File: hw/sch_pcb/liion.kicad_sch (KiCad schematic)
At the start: 64 parts, among them Q4 BC817-25, Q5 BC807-25, SW4 SKRTLAE010, U1 BQ34Z100, U13 BQ25628E, U2 SN74HC164D

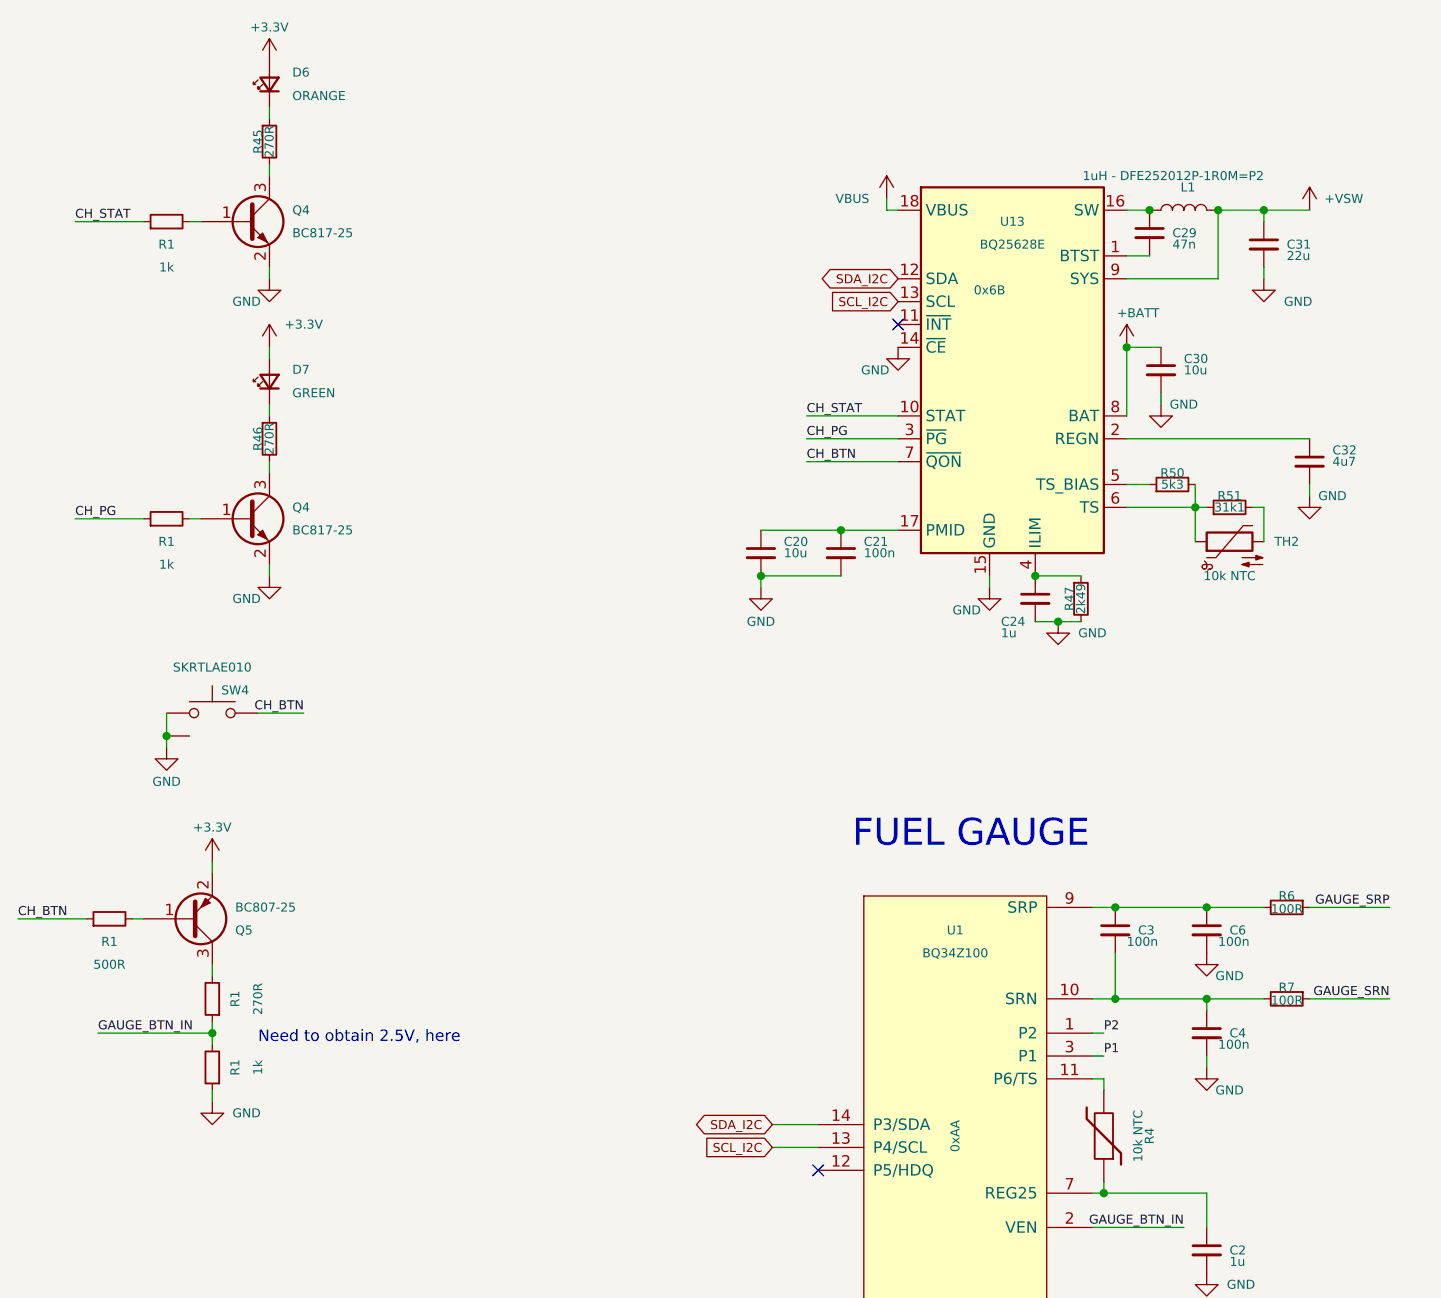
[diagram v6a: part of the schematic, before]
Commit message: minor updates, update kibot
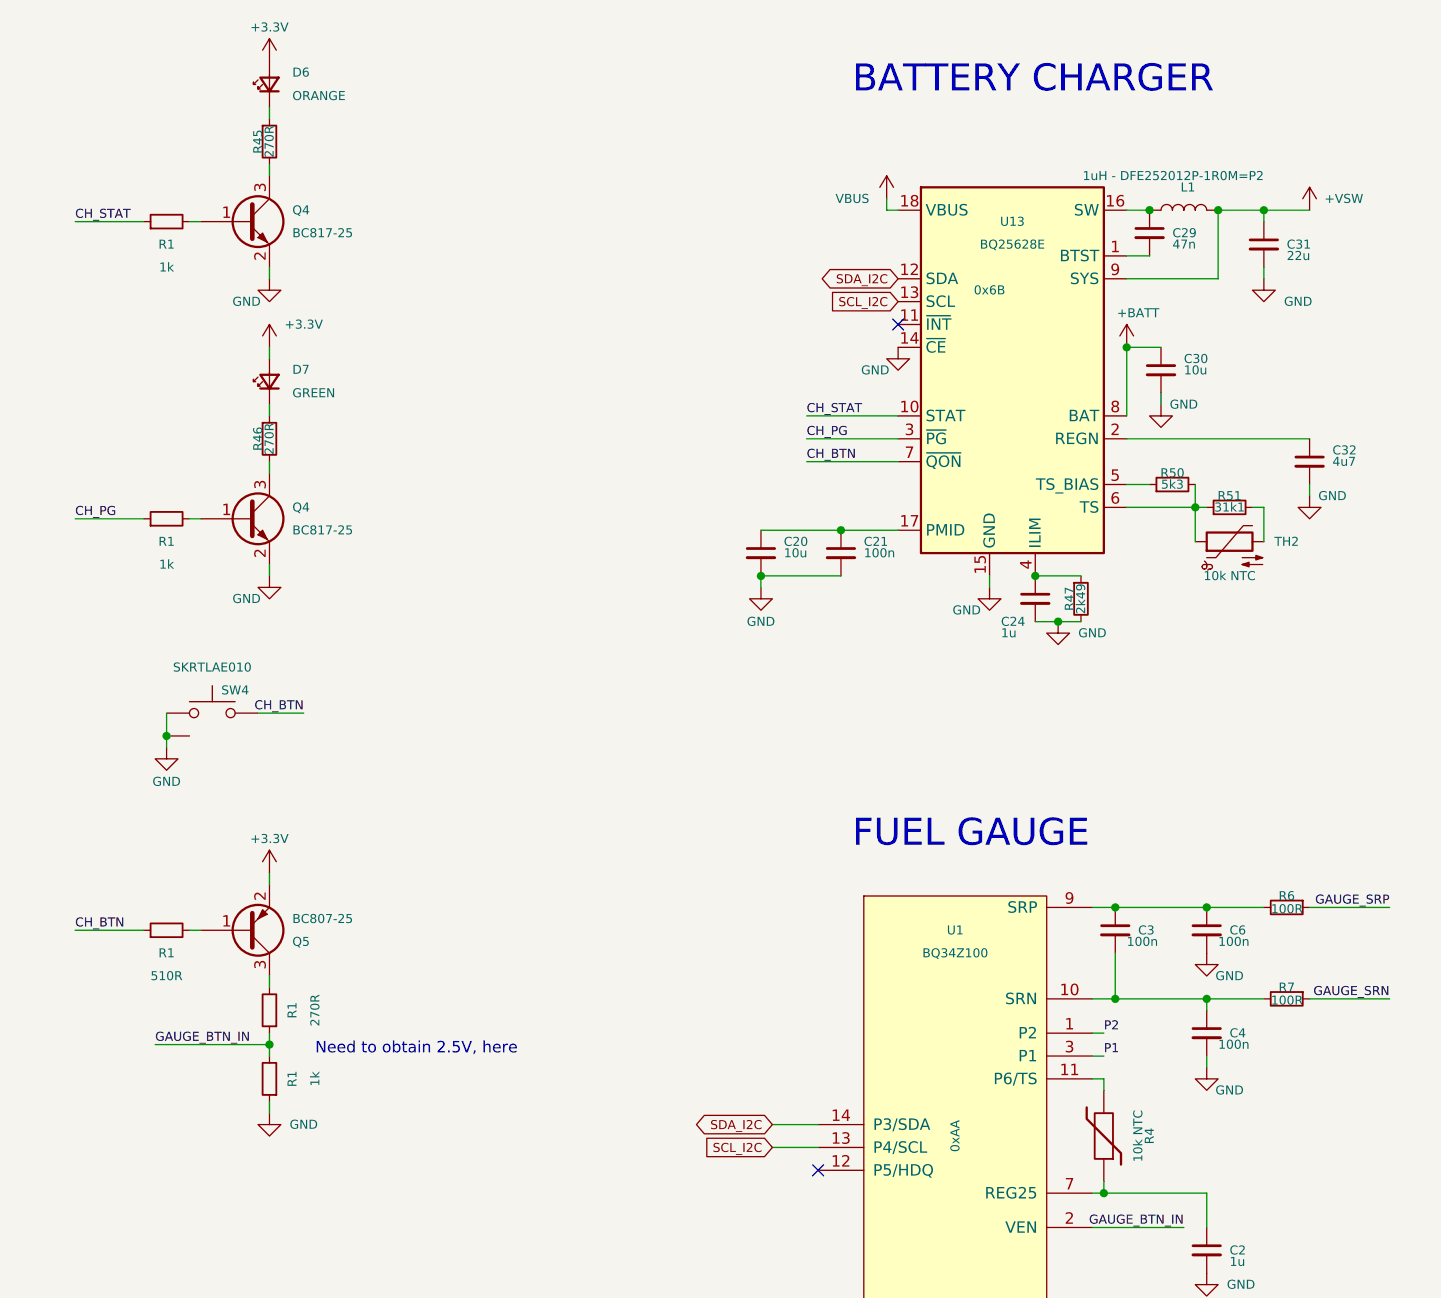
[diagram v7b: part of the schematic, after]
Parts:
- C29: UST_ID (none) -> 65482046462c6d9e72056b98
- D1, D2: UST_ID (none) -> 65481f96462c6d9e72056b54
- D3, D4, D5, D7: UST_ID (none) -> 65481f0c462c6d9e72056b3d
- D3, D4, D6: UST_ID (none) -> 65481fdd462c6d9e72056b6a
- R1: value 500R -> 510R; UST_ID (none) -> 5c70984512875079b91f8988
- R1, R10, R11, R12, R13, R45, R46, R9: UST_ID (none) -> 5c70984512875079b91f8983
- R47: UST_ID (none) -> 5c70984612875079b91f8991
- R50: UST_ID (none) -> 5fa0fc3e12875025b3977997
- R51: UST_ID (none) -> 5c70984712875079b91f8a8a
- SW4: UST_ID (none) -> 65481517462c6d9e720569b4
- U13: UST_ID (none) -> 65481a71462c6d9e72056aa4
- U2: UST_ID (none) -> 5c70984612875079b91f89ec
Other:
- note added: "BATTERY CHARGER"
- moved on the sheet: Q5, R1

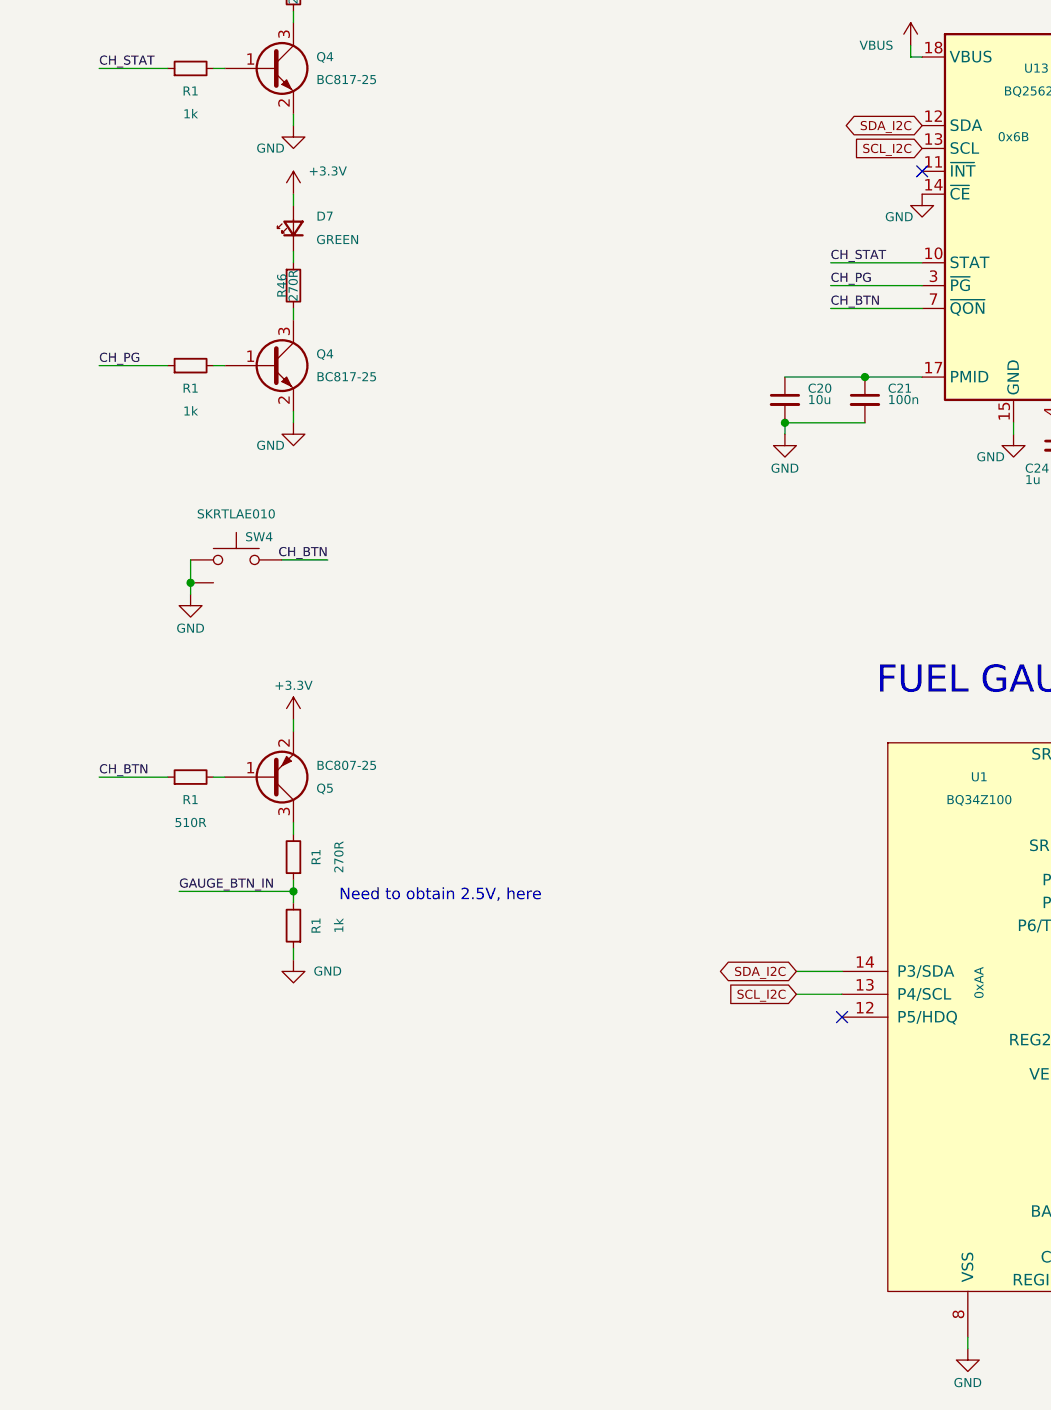
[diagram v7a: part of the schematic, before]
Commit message: updated power button connection
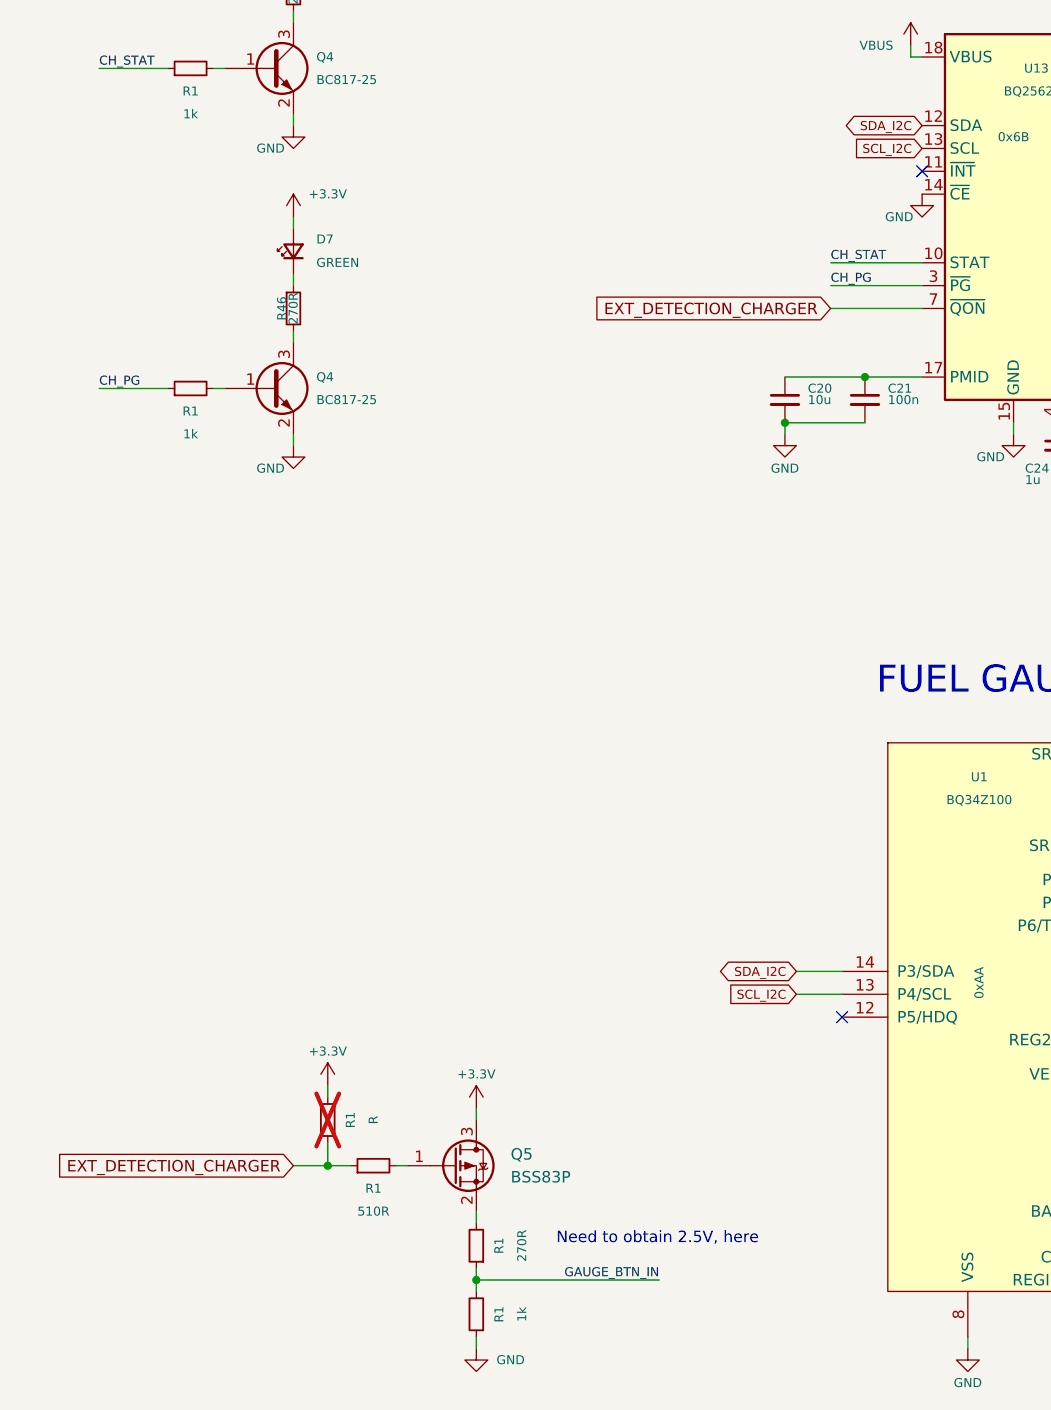
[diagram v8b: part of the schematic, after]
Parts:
- removed Q5: BC807-25, Package_TO_SOT_SMD:SOT-23-3, symbol Device:Q_PNP_BEC
- removed SW4: SKRTLAE010, Mlab_SW:SKRT, symbol MLAB_SW:SW_Push_shield
- added Q5: BSS83P, Package_TO_SOT_SMD:SOT-23, symbol Device:Q_PMOS_GSD
- added R1: R, Resistor_SMD:R_0805_2012Metric, symbol Device:R_Small
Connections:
- net +3.3V: now also Q5.3 (D), R1.2
- net at R1.2: now also Q5.1 (G)
- net at R1.2: now also Q5.2 (S)
- net CH_BTN renamed EXT_DETECTION_CHARGER
- net EXT_DETECTION_CHARGER: now also R1.1
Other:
- moved on the sheet: D7, Q4, R1, R46
